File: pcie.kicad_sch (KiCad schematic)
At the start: 22 parts, among them J10 OCuLink_x4_Amphenol_G14A42121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, J11 OCuLink_x4_Amphenol_G14A42121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

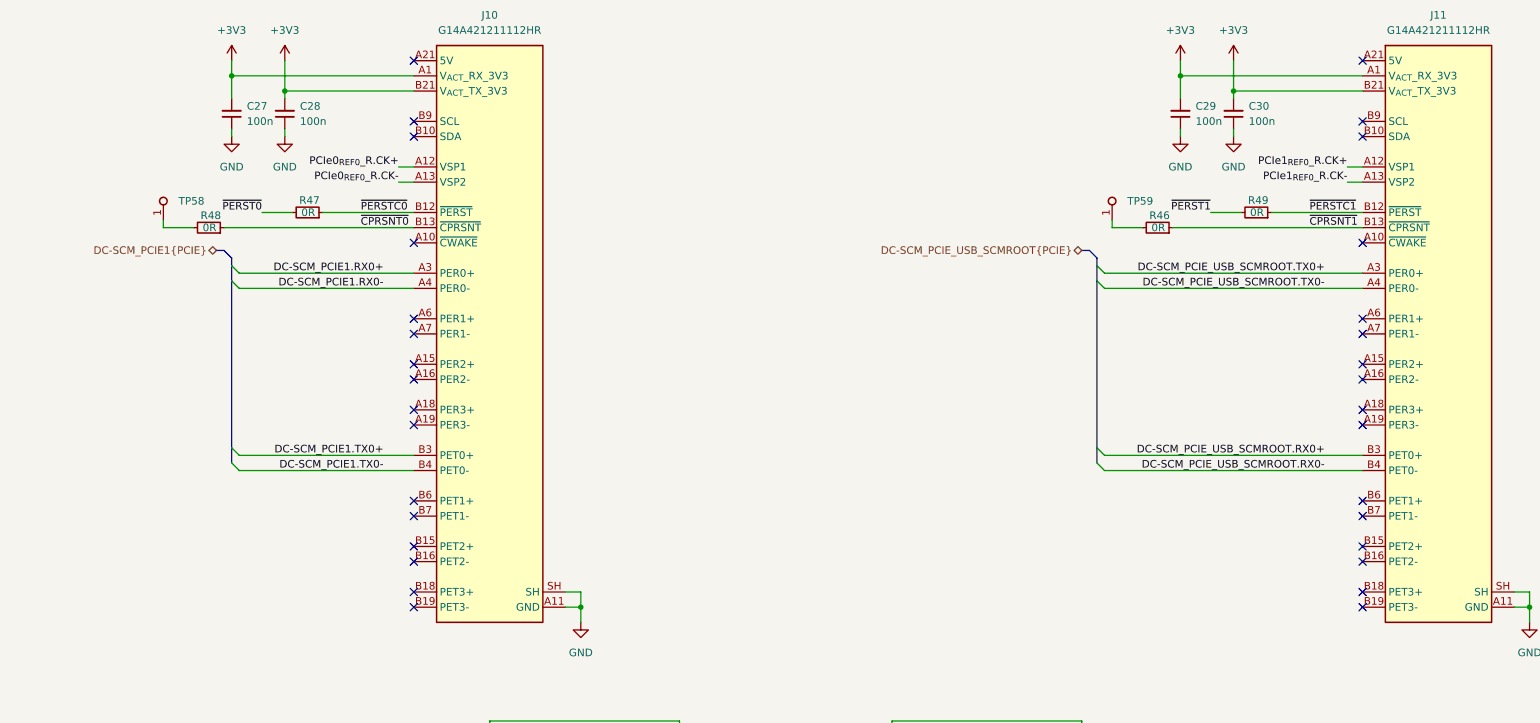
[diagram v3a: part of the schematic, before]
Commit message: [#92504] Wire second OCuLink and add testpads
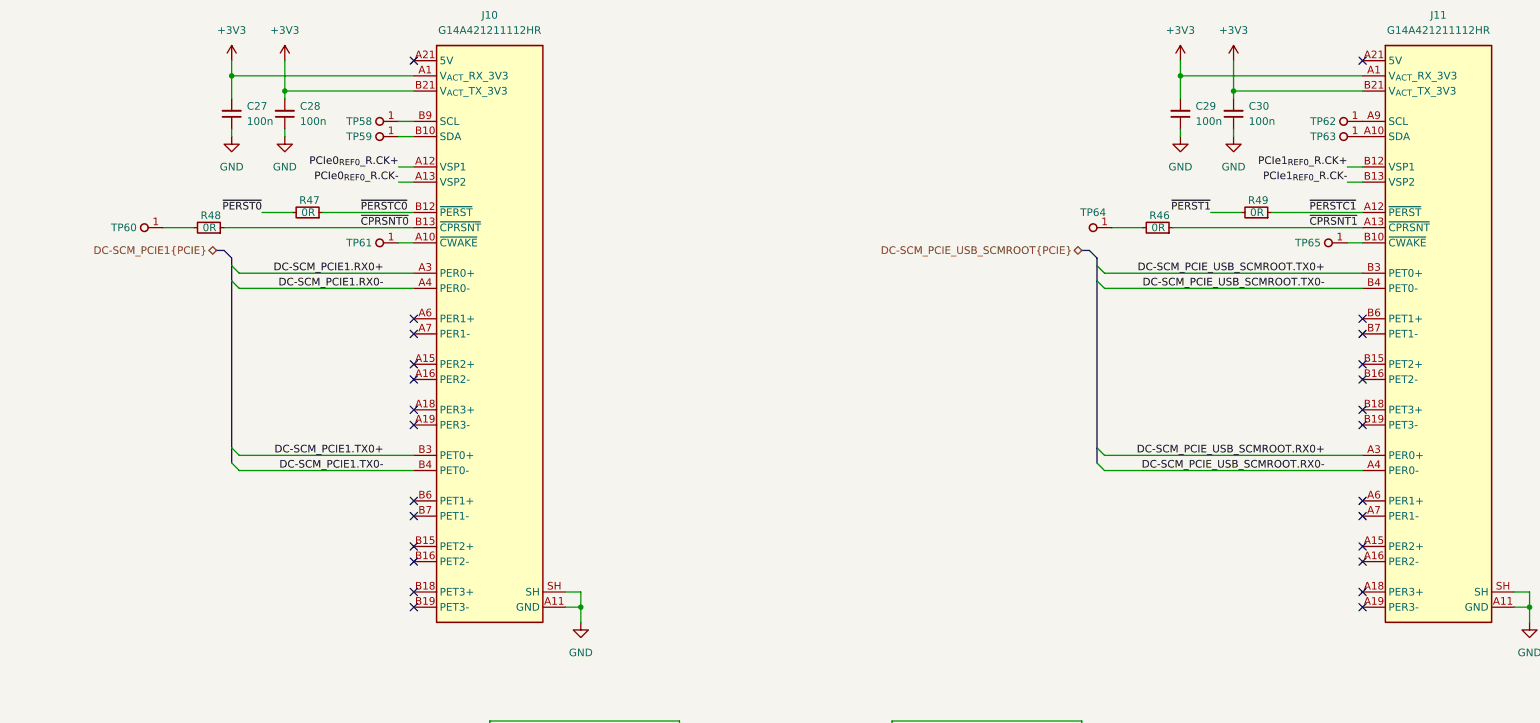
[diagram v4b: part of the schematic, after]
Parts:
- removed J11: OCuLink_x4_Amphenol_G14A421211112HR, antmicro-footprints:Amphenol_G14A421211112HR, symbol antmicroPciConnectors:OCuLink_x4_Amphenol_G14A421211112HR
- added J11: OCuLink_x4_Amphenol_G14A421211112HR_CUSTOM_device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, antmicro-footprints:Amphenol_G14A421211112HR, symbol antmicroPciConnectors:OCuLink_x4_Amphenol_G14A421211112HR_CUSTOM_device_side
- added TP59, TP60, TP61, TP62, TP63, TP65: TP_0.75mm_SMD, antmicro-footprints:TP_SMD_0.75mm, symbol antmicroTestPoints:TP_0.75mm_SMD
- renumbered TP59 to TP64
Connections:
- net +3V3: now also J11.A1 (V_{ACT}_RX_3V3), J11.B21 (V_{ACT}_TX_3V3)
- net DC-SCM_PCIE_USB_SCMROOT.RX0+: now also J11.A3 (PER0+)
- net DC-SCM_PCIE_USB_SCMROOT.RX0-: now also J11.A4 (PER0-)
- net DC-SCM_PCIE_USB_SCMROOT.TX0+: now also J11.B3 (PET0+)
- net DC-SCM_PCIE_USB_SCMROOT.TX0-: now also J11.B4 (PET0-)
- net GND: now also J11.A11 (GND), J11.A14 (GND), J11.A17 (GND), J11.A2 (GND), J11.A20 (GND), J11.A5 (GND), J11.A8 (GND), J11.B11 (GND), J11.B14 (GND), J11.B17 (GND), J11.B2 (GND), J11.B20 (GND), J11.B5 (GND), J11.B8 (GND), J11.SH
- net PCIe1_{REF0}_R.CK+: now also J11.B12 (VSP1)
- net PCIe1_{REF0}_R.CK-: now also J11.B13 (VSP2)
- net ~{CPRSNT1}: now also J11.A13 (~{CPRSNT})
- net ~{PERSTC1}: now also J11.A12 (~{PERST})
- net at R48.2: now also TP60.1; no longer TP58.1
- net at J10.A10 (~{CWAKE}): now also TP61.1
- net at J10.B10 (SDA): now also TP59.1
- net at J10.B9 (SCL): now also TP58.1
- new net: J11.A10 (SDA), TP63.1
- new net: J11.A21 (5V), J11.B1 (5V)
- new net: J11.A9 (SCL), TP62.1
- new net: J11.B10 (~{CWAKE}), TP65.1
- no-connect marks 32 -> 26
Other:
- moved on the sheet: TP58, TP64
